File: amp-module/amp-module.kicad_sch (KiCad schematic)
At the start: 27 parts, among them IC1 AD5245BRJZ10-RL7, U5 TPA3221DDVR

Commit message: cleanup footprints and layout
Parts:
- C9: value 1uf GMK316BJ105KL 100v -> 1uf
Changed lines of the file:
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@@
 			)
 		)
-		(property "Value" "1uf GMK316BJ105KL 100v"
+		(property "Value" "1uf"
 			(at 112.776 29.972 90)
 			(effects

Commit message: finish everything
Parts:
- removed R7: 10kΩ, PCM_JLCPCB:R_0603, symbol PCM_JLCPCB-Resistors:0402,10kΩ
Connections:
- net GND: no longer IC1.5 (SDA), R3.1, U1.1 (GP1)
- new net: IC1.5 (SDA), R3.1, U1.1 (GP1)
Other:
- note removed: "Address 1110"

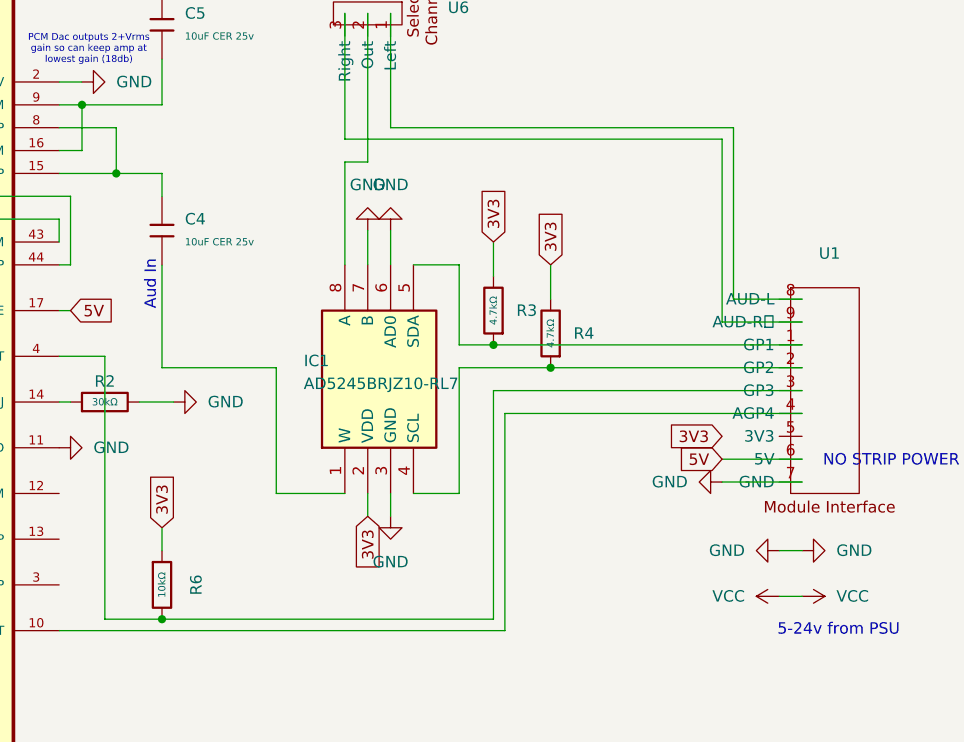
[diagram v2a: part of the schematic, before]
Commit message: replace amp with screw pot
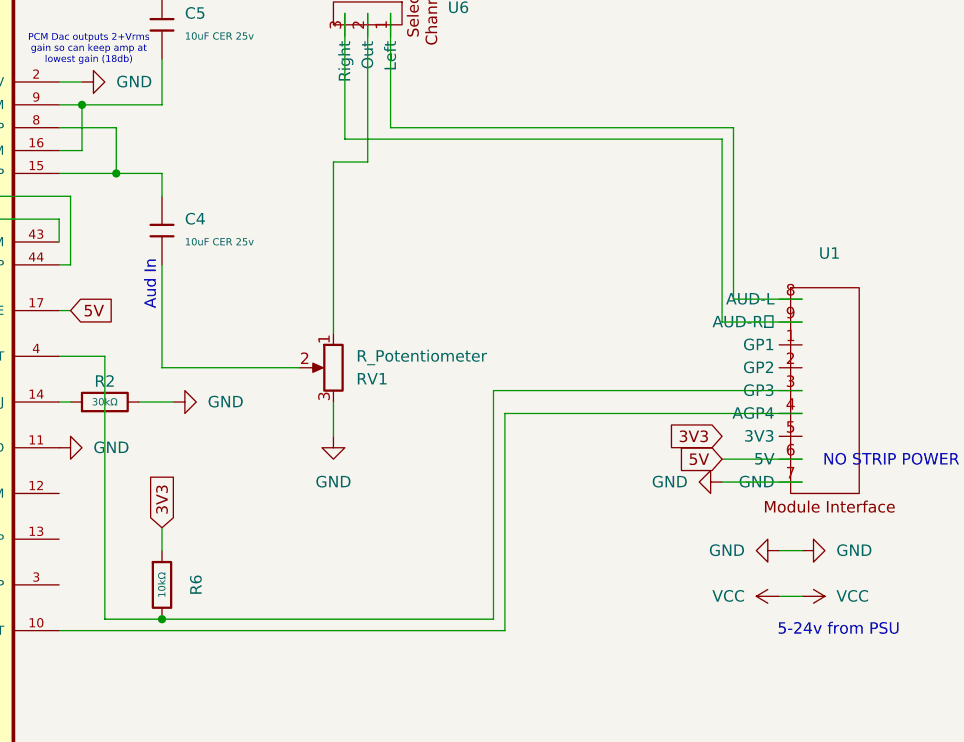
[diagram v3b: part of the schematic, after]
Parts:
- removed IC1: AD5245BRJZ10-RL7, Imported:SOT65P280X145-8N, symbol AD5245BRJZ10-RL7:AD5245BRJZ10-RL7
- removed R3, R4: 4.7kΩ, PCM_JLCPCB:R_0603, symbol PCM_JLCPCB-Resistors:0402,4.7kΩ
- added RV1: R_Potentiometer, Imported:601030_AVX, symbol Device:R_Potentiometer
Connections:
- net GND: now also RV1.3
- net at U6.2 (Out): now also RV1.1
- net at C4.1: now also RV1.2
